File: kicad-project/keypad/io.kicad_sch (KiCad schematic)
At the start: 18 parts, among them SW1 RotaryEncoder, SW2 RotaryEncoder, SW25 SW_RST

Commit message: correct schematic
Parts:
- added C9: 1uF, Capacitor_SMD:C_0603_1608Metric, symbol PutRocketLab_RCL:C_Small
- added SW25: SW_RST, Button_Switch_THT:SW_PUSH_6mm, symbol Switch:SW_SPST
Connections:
- net GND: now also C9.2, SW25.1 (A)
- new net DTR: C9.1, SW25.2 (B)
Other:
- note added: "Manual program"
- moved on the sheet: 1, C9, D26, D27, R16, R17, R18, RV1, SW25

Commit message: fix board, update production files
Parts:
- C9: footprint Capacitor_SMD:C_0603_1608Metric -> Capacitor_SMD:C_0603_1608Metric_Pad1.08x0.95mm_HandSolder
- SW25: value SW_RST -> SW_DTR
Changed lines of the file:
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@@
       (effects (font (size 1.27 1.27)) (justify left))
     )
-    (property "Footprint" "Capacitor_SMD:C_0603_1608Metric" (at 64.77 127 0)
+    (property "Footprint" "Capacitor_SMD:C_0603_1608Metric_Pad1.08x0.95mm_HandSolder" (at 64.77 127 0)
       (effects (font (size 1.27 1.27)) hide)
     )
@@
       (effects (font (size 1.27 1.27)) (justify left))
     )
-    (property "Footprint" "Capacitor_SMD:C_0603_1608Metric" (at 124.46 45.72 0)
+    (property "Footprint" "Capacitor_SMD:C_0603_1608Metric_Pad1.08x0.95mm_HandSolder" (at 124.46 45.72 0)
       (effects (font (size 1.27 1.27)) hide)
     )
@@
       (effects (font (size 1.27 1.27)) (justify left))
     )
-    (property "Footprint" "Capacitor_SMD:C_0603_1608Metric" (at 129.54 109.22 0)
+    (property "Footprint" "Capacitor_SMD:C_0603_1608Metric_Pad1.08x0.95mm_HandSolder" (at 129.54 109.22 0)
       (effects (font (size 1.27 1.27)) hide)
     )
@@
       (effects (font (size 1.27 1.27)) (justify left))
     )
-    (property "Footprint" "Capacitor_SMD:C_0603_1608Metric" (at 64.77 109.22 0)
+    (property "Footprint" "Capacitor_SMD:C_0603_1608Metric_Pad1.08x0.95mm_HandSolder" (at 64.77 109.22 0)
       (effects (font (size 1.27 1.27)) hide)
     )
@@
       (effects (font (size 1.27 1.27)) (justify left))
     )
-    (property "Footprint" "Capacitor_SMD:C_0603_1608Metric" (at 176.53 44.45 0)
+    (property "Footprint" "Capacitor_SMD:C_0603_1608Metric_Pad1.08x0.95mm_HandSolder" (at 176.53 44.45 0)
       (effects (font (size 1.27 1.27)) hide)
     )
@@
       (effects (font (size 1.27 1.27)) (justify left))
     )
-    (property "Footprint" "Capacitor_SMD:C_0603_1608Metric" (at 129.54 127 0)
+    (property "Footprint" "Capacitor_SMD:C_0603_1608Metric_Pad1.08x0.95mm_HandSolder" (at 129.54 127 0)
       (effects (font (size 1.27 1.27)) hide)
     )
@@
       (effects (font (size 1.27 1.27)))
     )
-    (property "Value" "SW_RST" (at 168.91 35.56 0)
-      (effects (font (size 1.27 1.27)))
-    )
+    (property "Value" "SW_DTR" (at 168.91 35.56 0)
+      (effects (font (size 1.27 1.27)))
+    )

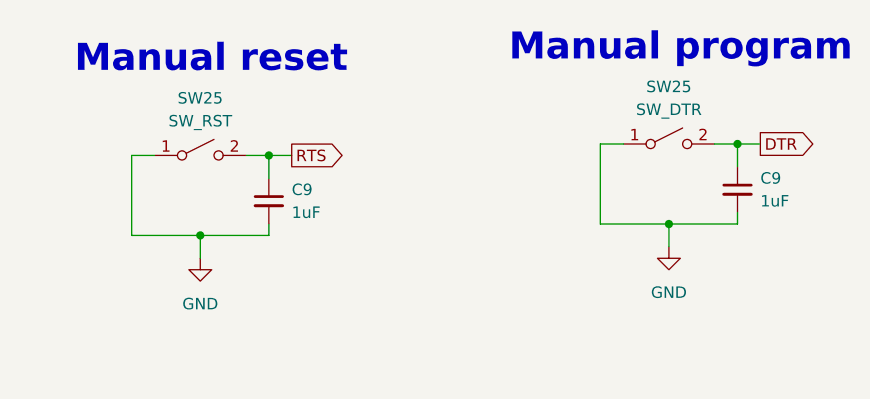
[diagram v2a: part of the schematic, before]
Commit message: update schematic
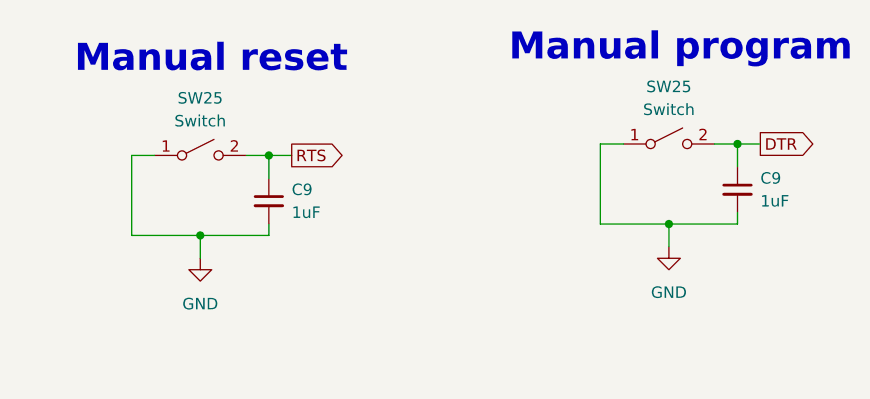
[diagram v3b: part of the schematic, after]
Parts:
- SW25: value SW_RST -> Switch
- SW25: value SW_DTR -> Switch
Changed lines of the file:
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@@
       (effects (font (size 1.27 1.27)))
     )
-    (property "Value" "SW_RST" (at 116.84 36.83 0)
+    (property "Value" "Switch" (at 116.84 36.83 0)
       (effects (font (size 1.27 1.27)))
     )
@@
       (effects (font (size 1.27 1.27)))
     )
-    (property "Value" "SW_DTR" (at 168.91 35.56 0)
-      (effects (font (size 1.27 1.27)))
-    )
+    (property "Value" "Switch" (at 168.91 35.56 0)
+      (effects (font (size 1.27 1.27)))
+    )
